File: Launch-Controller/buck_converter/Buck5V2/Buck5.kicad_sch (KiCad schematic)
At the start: 13 parts, among them J1 Conn_01x10_Socket, U1 LM2596S-5

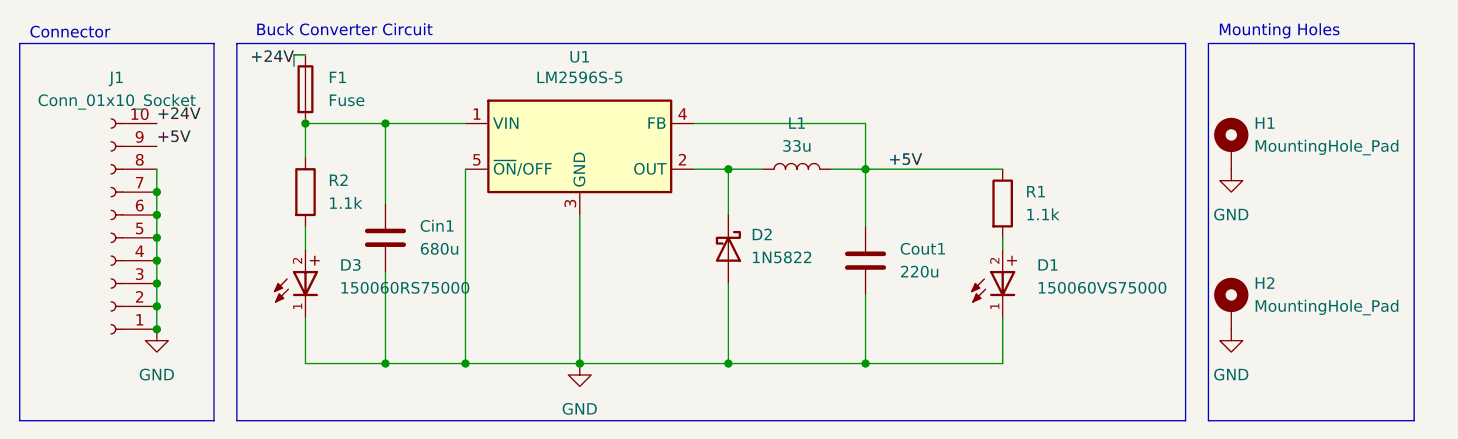
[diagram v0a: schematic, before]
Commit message: redone buck converter
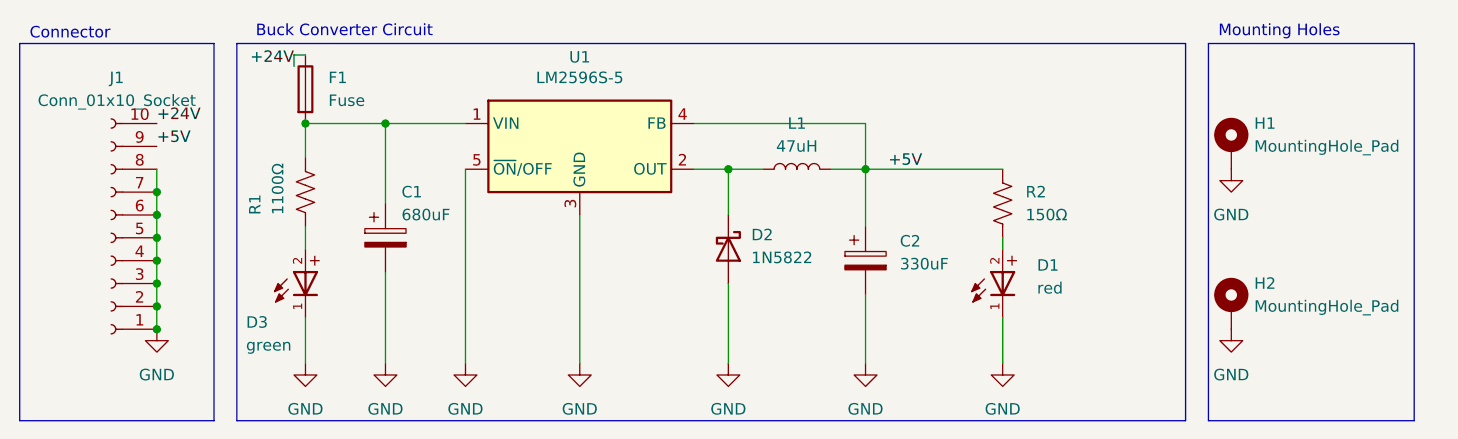
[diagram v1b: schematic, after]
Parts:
- removed Cin1: 680u, KiCad:CAPAE660X800N, symbol Library:C
- removed Cout1: 220u, footprints:CAP_YX_6P3X11_RUB, symbol Library:C
- removed R1, R2: 1.1k, RMCF0805JT1K10:RESC2012X65N, symbol Library:R
- added C1: 680uF, Library:CAPAE660X800N, symbol Device:C_Polarized
- added C2: 330uF, Capacitor_THT:CP_Radial_D8.0mm_P3.50mm, symbol Device:C_Polarized
- added R1: 1100Ω, Resistor_SMD:R_1210_3225Metric_Pad1.30x2.65mm_HandSolder, symbol Device:R_US
- added R2: 150Ω, Resistor_SMD:R_0805_2012Metric_Pad1.20x1.40mm_HandSolder, symbol Device:R_US
- D1: value 150060VS75000 -> red; footprint WL-SMCW_0603:WL-SMCW_0603 -> LED_SMD:LED_1206_3216Metric_Pad1.42x1.75mm_HandSolder
- D3: value 150060RS75000 -> green; footprint WL-SMCW_0603:WL-SMCW_0603 -> LED_SMD:LED_0603_1608Metric_Pad1.05x0.95mm_HandSolder
- J1: footprint 10pin Socket:PRECI-DIP_310-87-110-41-001101 -> Library:PRECI-DIP_310-87-110-41-001101
- L1: value 33u -> 47uH; footprint NLCV32T_330K_EF:INDM3225X240N -> Library:output inductor
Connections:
- net +5V: now also C2.1, R2.1
- net GND: now also C1.2, C2.2
- net at F1.2, U1.1 (VIN): now also C1.1, R1.1
- net at D1.2: now also R2.2
- net at D3.2: now also R1.2
